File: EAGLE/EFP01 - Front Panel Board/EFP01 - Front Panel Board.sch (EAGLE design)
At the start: 150 parts, among them J1 PWRBTN, J16 S8B-PH-SM4, J17 S8B-PH-SM4, J18 S6B-PH-SM4, J2 ESTOP, J20 Intel EDISON, J3 USB-A(2.0), J5 LCD, J6 S8B-PH-SM4, J7 USB-B, Q2 25MHz, U1 74LVC1T45, U10 FT231XS-R, U11 74LVC1T45, U12 74LVC1T45, U13 74LVC1T45, U14 74LVC1T45, U15 74LVC1T45, U17 OR, U18 MIC2026-1YM, U19 MIC2026-1YM, U2 74LVC1T45, U20 OR, U21 74LVC1T45, U22 74LVC1T45, U23 74LVC1T45, U24 74LVC1T45, U25 74LVC1T45, U26 74LVC1T45, U27 74LVC1T45, U28 74LVC1T45, U3 93LC66A, U30 74LVC1T45, U4 LAN9514, U5 74LVC1T45, U6 74LVC1T45, U7 74LVC1T45, U8 74LVC1T45, U9 SP3485

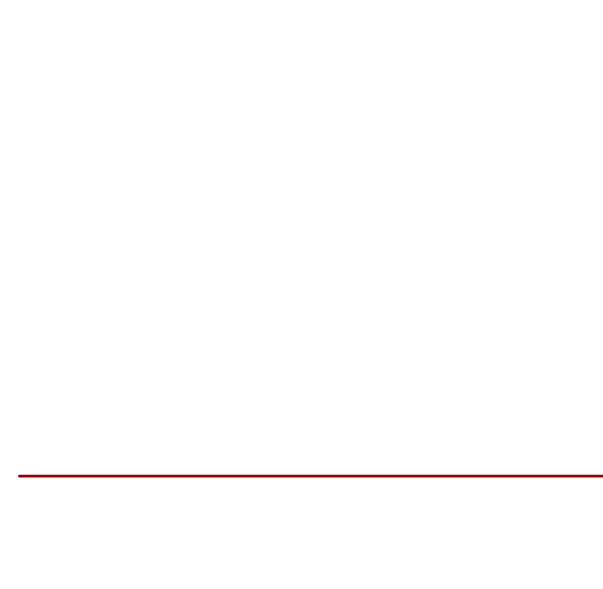
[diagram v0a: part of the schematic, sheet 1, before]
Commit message: Minor changes to EFP01.  One show-stopper DRC error (overlapping traces).  Added logo and P/N.  Other misc. tweaks.  Generated Gerbers for Rev--.
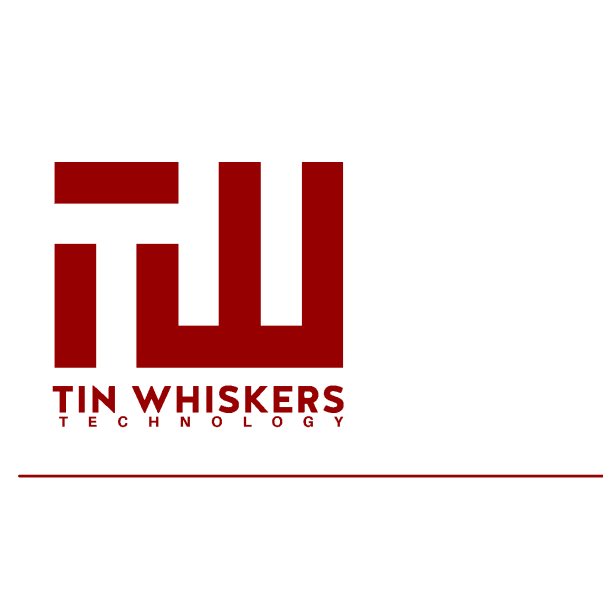
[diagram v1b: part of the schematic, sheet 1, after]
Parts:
- added U$1: TIN-WHISKERSTSTOP, !tin-whiskers-logo:TIN-WHISKERSTSTOP
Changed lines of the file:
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@@
 <?xml version="1.0" encoding="utf-8"?>
 <!DOCTYPE eagle SYSTEM "eagle.dtd">
-<eagle version="7.4.0">
+<eagle version="7.3.0">
 <drawing>
 <settings>
@@
 <attribute name="PARTNO" value="GMK107BJ104KAHT"/>
 </part>
+<part name="U$1" library="!tin-whiskers-logo" deviceset="TIN-WHISKERS" device="TSTOP"/>
 </parts>
 <sheets>
@@
 <attribute name="PARTNO" x="66.04" y="231.14" size="1.778" layer="96" rot="R90" display="off"/>
 </instance>
+<instance part="U$1" gate="G$1" x="7.62" y="33.02"/>
 </instances>
 <busses>

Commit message: Changing resistor tolerances to 1%
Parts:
- R13: value 12.4K -> 12.4K 1%
- R35: value 12K -> 12K 1%
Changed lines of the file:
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@@
 </part>
 <part name="P+19" library="supply1" deviceset="+3V3" device=""/>
-<part name="R13" library="TinWhiskers" deviceset="CPL-RES-0603-12.4K-0.1W" device="" value="12.4K">
+<part name="R13" library="TinWhiskers" deviceset="CPL-RES-0603-12.4K-0.1W" device="" value="12.4K 1%">
 <attribute name="PARTNO" value="RC0603FR-0712K4L"/>
 </part>
@@
 <part name="+3V29" library="supply1" deviceset="+3V3" device=""/>
 <part name="SUPPLY75" library="TinWhiskers" deviceset="GND" device=""/>
-<part name="R35" library="TinWhiskers" deviceset="CPL-RES-0603-12K-0.1W" device="" value="12K">
+<part name="R35" library="TinWhiskers" deviceset="CPL-RES-0603-12K-0.1W" device="" value="12K 1%">
 <attribute name="PARTNO" value="RC0603FR-0712KL"/>
 </part>
